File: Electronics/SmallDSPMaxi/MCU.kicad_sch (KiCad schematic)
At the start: 54 parts, among them J21 Header, J22 Header, J23 Header, J24 Header, Q2 2N7002, Q3 2N7002, Q4 2N7002, SW3 TS-1187A-B-A-B, U15 STM32F030C8Tx, Y2 8MHz

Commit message: Adds final state of Maxi rev 1.0 and unbalanced IO boards rev 1.0.
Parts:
- removed D? (x6): P6SMB6.8CA, Diode_SMD:D_SMB, symbol Device:D_TVS
- added U? (x2): H5VU25U, Package_DFN_QFN:Diodes_UDFN-10_1.0x2.5mm_P0.5mm, symbol 1_Project_Symbols:H5VU25U
- renumbered C110 to C112, C112 to C114, C113 to C115, C114 to C116, C115 to C117, C117 to C119, C118 to C120, JP1 to JP2, R80 to R72, R82 to R75, R89 to R85, R90 to R86, R92 to R88, R93 to R89, R95 to R91, R96 to R92, TP22 to TP23, TP23 to TP24, TP24 to TP25, TP25 to TP26, U15 to U19
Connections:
- net +3V3: now also U?.1
- net Earth_Protective: now also U?.3 (VSS), U?.3 (VSS), U?.8 (VSS), U?.8 (VSS)
- net SWCLK: now also U?.5
- net SWDIO: now also U?.2
- net ~{RST DSP}: now also U?.2
- net ~{RST}: now also U?.1, U?.4
- no-connect marks 16 -> 18
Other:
- moved on the sheet: JP2, R72, R75, SW3

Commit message: Maxi: Replaces STM32 programming pin header with WE RedFit connectorand fixes minor issues. Adds driver for AKM AK4619 Codec and STM32CubeIDE workspace for Maxi firmware.
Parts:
- J23: footprint Connector_PinHeader_1.27mm:PinHeader_2x07_P1.27mm_Vertical -> 1_Project_Footprints:WE_WR-WST_REDFIT-14_Debugging; Manufacturer Amphenol FCI -> -; Part Number 20021111-00014T1LF -> -
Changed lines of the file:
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@@
   (title_block
     (title "SmallDSP Maxi")
-    (date "2024-01-06")
-    (rev "1.0")
+    (date "2024-02-19")
+    (rev "1.1")
     (company "Till Heuer")
   )
@@
       (effects (font (size 1.27 1.27)))
     )
-    (property "Footprint" "Connector_PinHeader_1.27mm:PinHeader_2x07_P1.27mm_Vertical" (at 223.52 124.46 0)
+    (property "Footprint" "1_Project_Footprints:WE_WR-WST_REDFIT-14_Debugging" (at 223.52 124.46 0)
       (effects (font (size 1.27 1.27)) hide)
     )
@@
       (effects (font (size 1.27 1.27)) hide)
     )
-    (property "Manufacturer" "Amphenol FCI" (at 223.52 124.46 0)
-      (effects (font (size 1.27 1.27)) hide)
-    )
-    (property "Part Number" "20021111-00014T1LF" (at 223.52 124.46 0)
-      (effects (font (size 1.27 1.27)) hide)
-    )
+    (property "Manufacturer" "-" (at 223.52 124.46 0)
+      (effects (font (size 1.27 1.27)) hide)
+    )
+    (property "Part Number" "-" (at 223.52 124.46 0)
+      (effects (font (size 1.27 1.27)) hide)
+    )

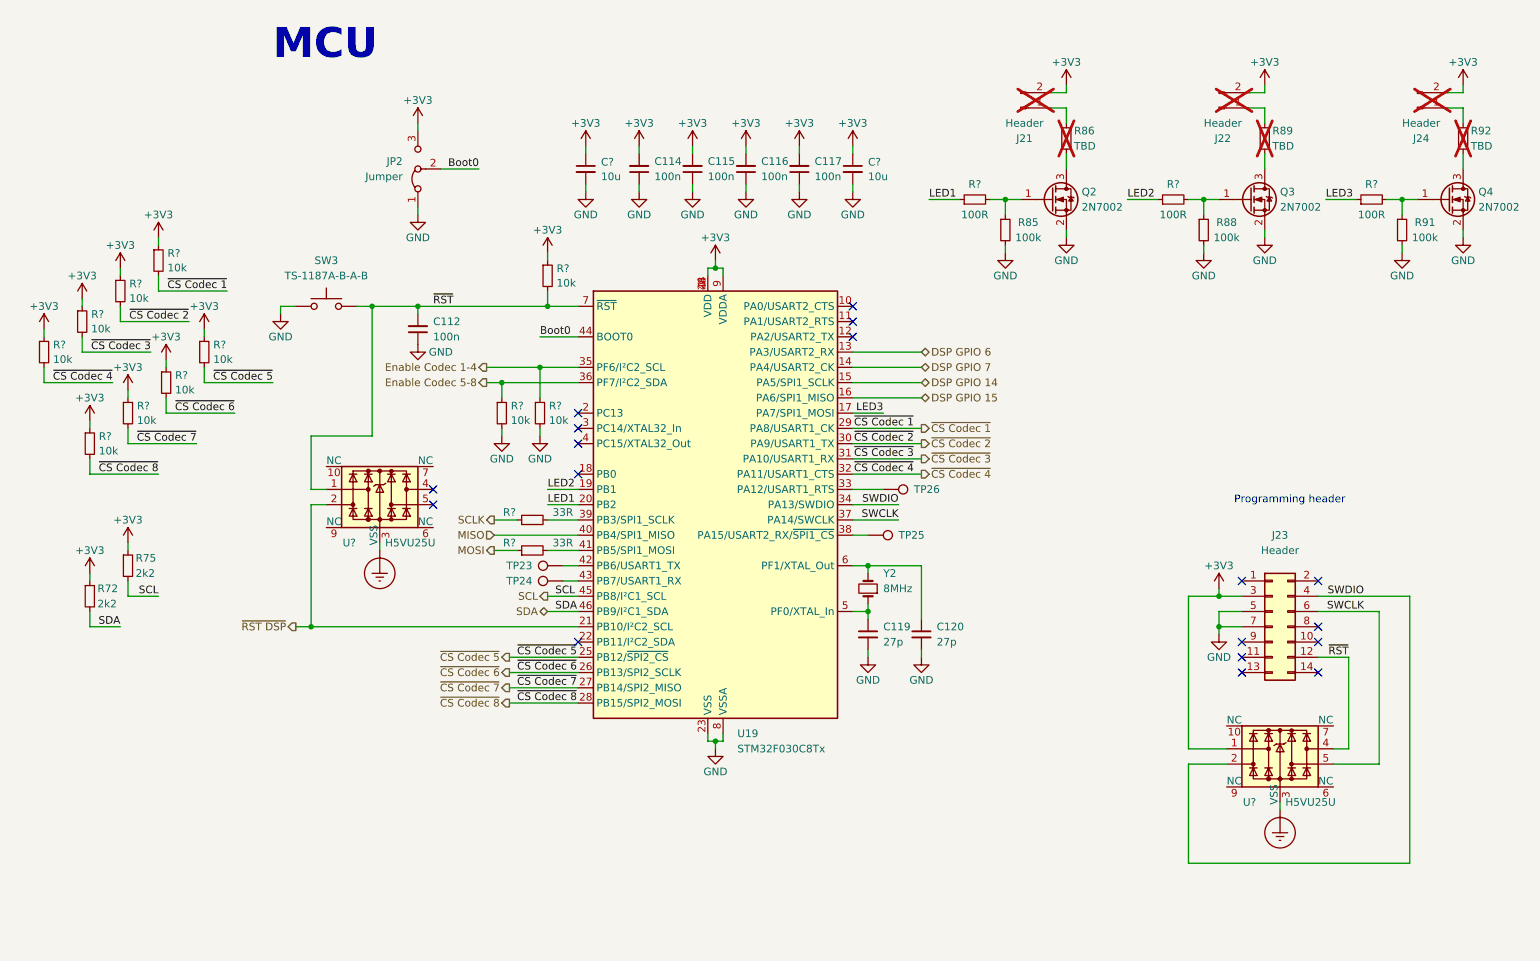
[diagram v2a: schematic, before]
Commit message: Adds AES17 measurements for rev1 of maxi. adds first iteration of maxi firmware. prototype now functional. adds mechanical information such as pcb 3d models and datasheets for psu and power switch, -connector.
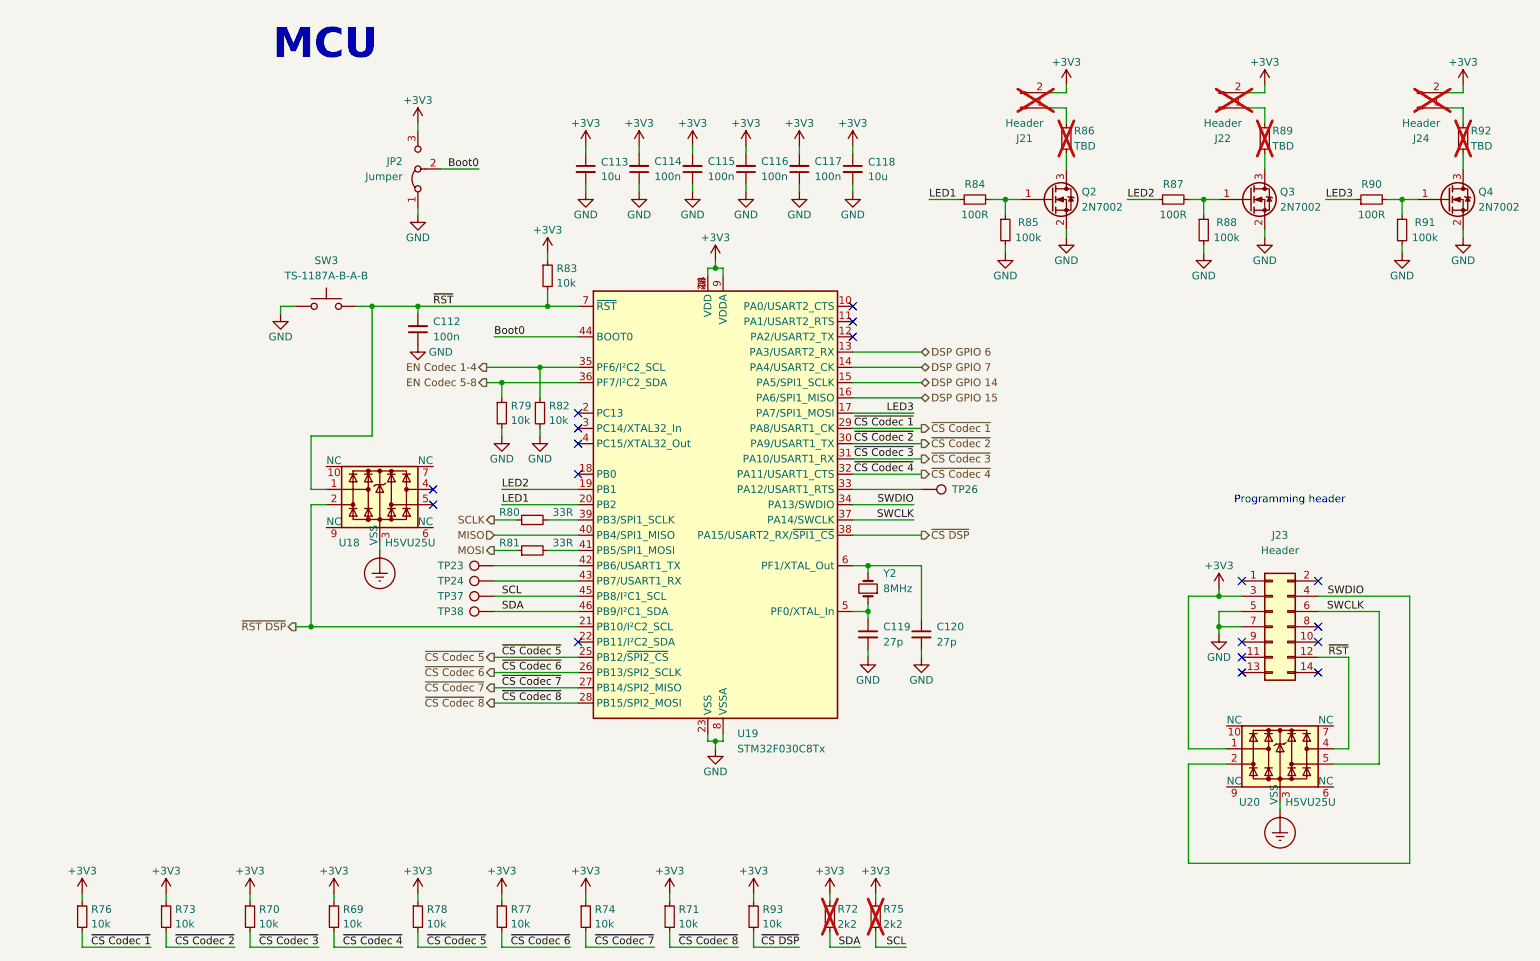
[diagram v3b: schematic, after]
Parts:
- removed TP25: TestPoint, TestPoint:TestPoint_Pad_D1.0mm, symbol Connector:TestPoint
- added R93: 10k, Resistor_SMD:R_0402_1005Metric, symbol Device:R_Small
- added TP37, TP38: TestPoint, TestPoint:TestPoint_Pad_D1.0mm, symbol Connector:TestPoint
- R72, R75: now not fitted
- gave numbers to parts that had none: 20
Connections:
- net +3V3: now also R93.1
- net SCL: now also TP37.1
- net SDA: now also TP38.1
- net ~{CS DSP}: now reaches U19.38 (PA15/USART2_RX/~{SPI1_CS})
- net ~{CS DSP}: now also R93.2
- net Enable Codec 1-4 renamed EN Codec 1-4
- net Enable Codec 5-8 renamed EN Codec 5-8
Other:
- moved on the sheet: R69, R70, R71, R73, R74, R76, R77, R78, TP23, TP24, TP26
